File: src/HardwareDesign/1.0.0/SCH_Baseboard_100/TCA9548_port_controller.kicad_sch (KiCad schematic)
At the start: 24 parts, among them IC4 TCA9548ARGER

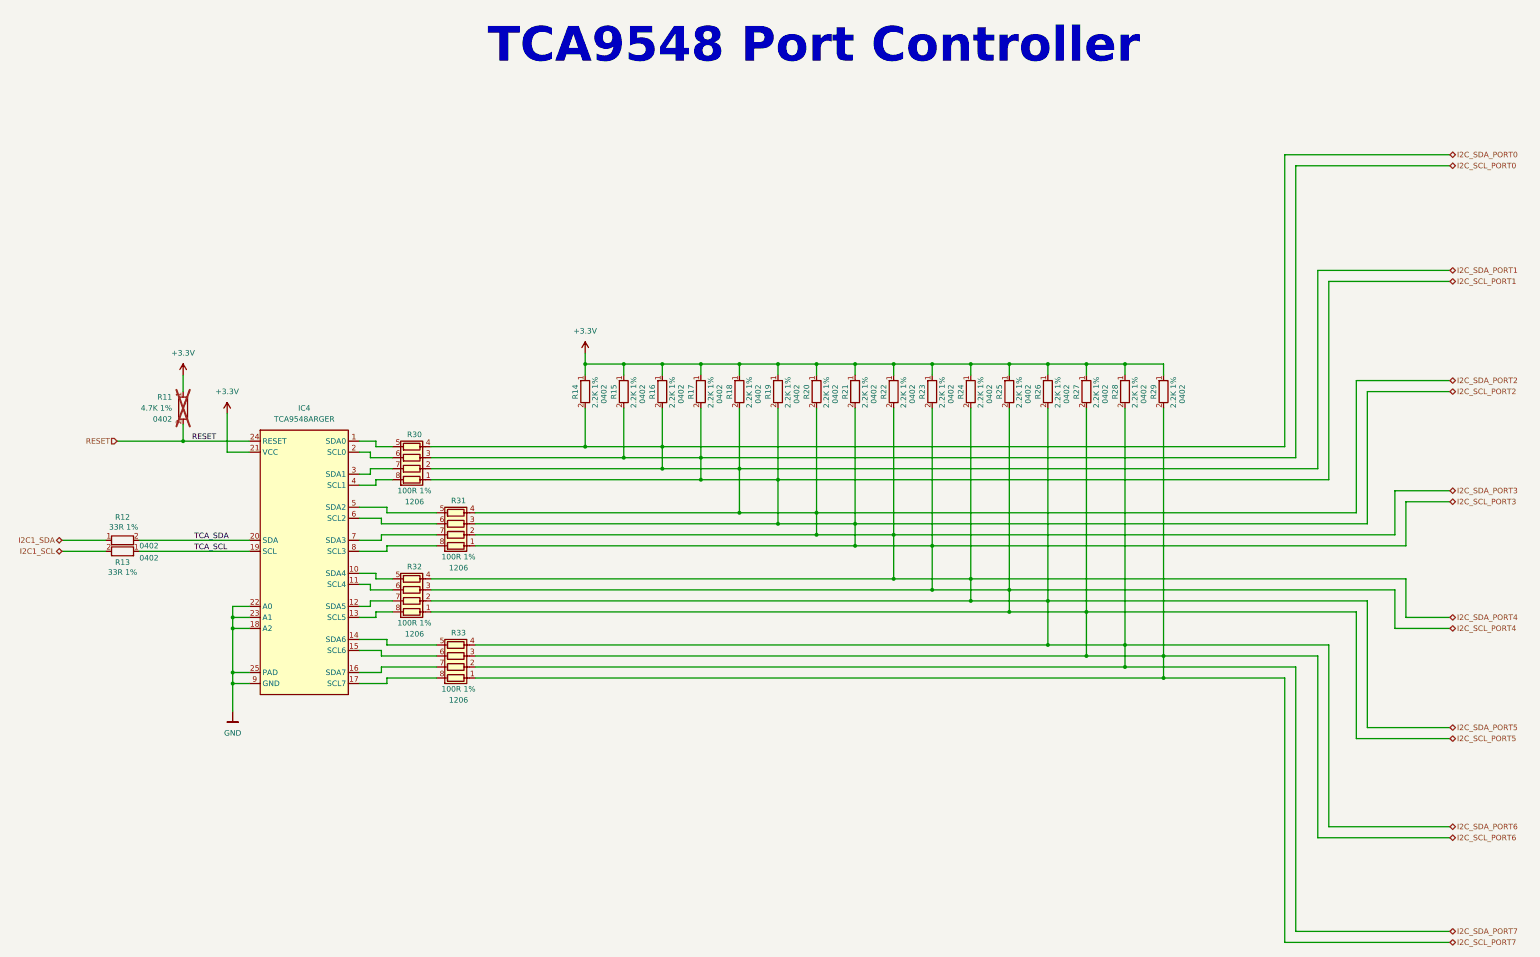
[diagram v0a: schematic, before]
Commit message: Add bladecore to design
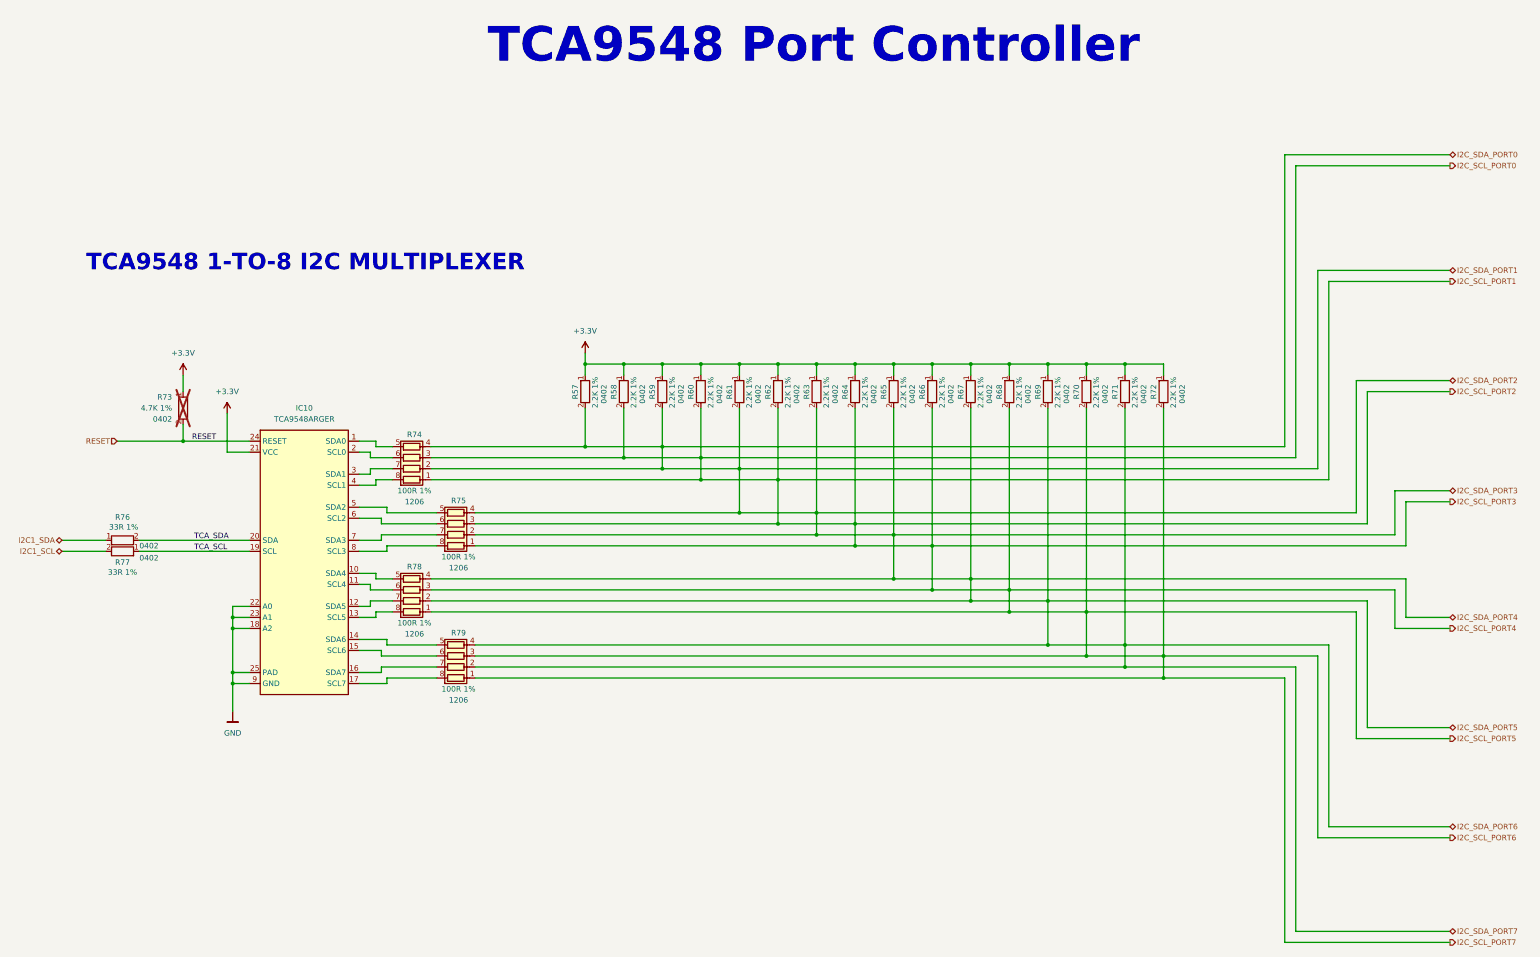
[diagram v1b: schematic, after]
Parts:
- renumbered IC4 to IC10, R14 to R57, R15 to R58, R16 to R59, R17 to R60, R18 to R61, R19 to R62, R20 to R63, R21 to R64, R22 to R65, R23 to R66, R24 to R67, R25 to R68, R26 to R69, R27 to R70, R28 to R71, R29 to R72, R11 to R73, R30 to R74, R31 to R75, R12 to R76, R13 to R77, R32 to R78, R33 to R79
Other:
- note added: "TCA9548 1-TO-8 I2C MULTIPLEXER"
